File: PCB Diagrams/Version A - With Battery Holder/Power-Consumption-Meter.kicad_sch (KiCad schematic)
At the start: 36 parts, among them J1 Jack_DC, J10 01x02, J11 01x02, J12 01x02, J13 01x02, J2 01x02, J3 01x02, J4 USB_A, J5 Jack_DC, J6 Jack_DC, J7 USB_B_Mini, J8 USB_B_Micro, J9 01x04, SW1 SW_SPDT, SW2 SW_Push, U1 INA219_Module, U2 Display_5641BS

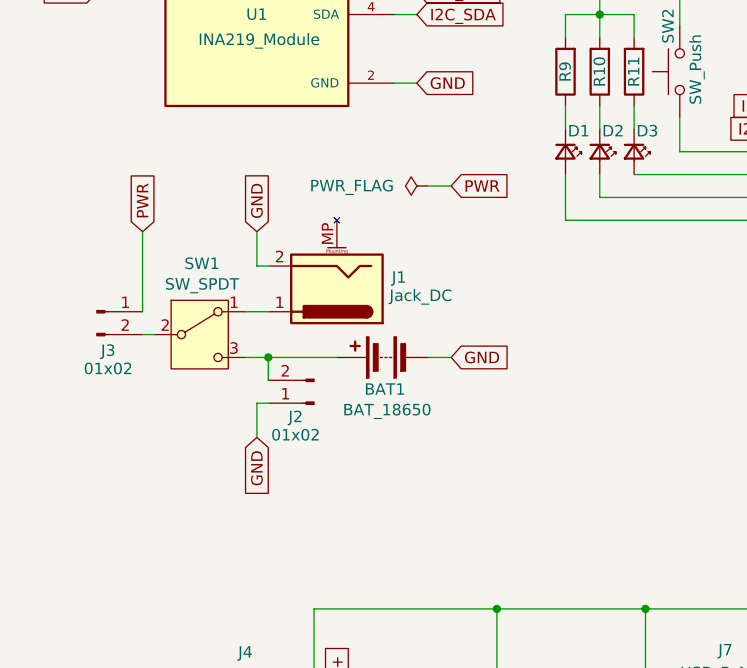
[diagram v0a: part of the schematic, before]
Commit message: update PCB connectors
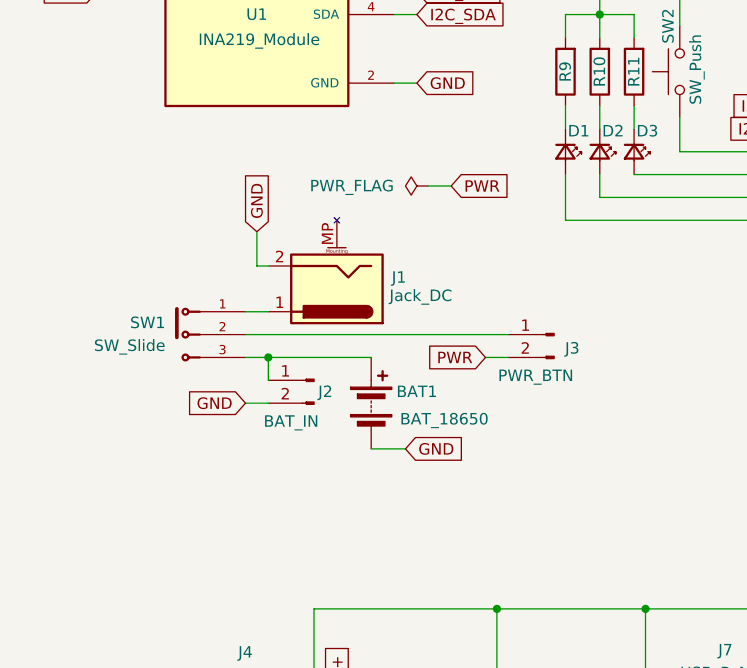
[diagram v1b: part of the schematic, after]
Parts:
- removed SW1: SW_SPDT, Button_Switch_THT:SW_Slide_SPDT_Straight_CK_OS102011MS2Q, symbol Switch:SW_SPDT
- added SW1: SW_Slide, Custom:Switch_Slide_SPDT_Straight_TE_1825159_1, symbol Custom:Switch_Slide_SPDT_Straight_TE_1825159_1
- J2: value 01x02 -> BAT_IN
- J3: value 01x02 -> PWR_BTN
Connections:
- net GND: now also J2.2 (Pin_2); no longer J2.1 (Pin_1)
- net PWR: now also J3.2 (Pin_2); no longer J3.1 (Pin_1)
- net at J1.1: now also SW1.1
- net at BAT1.1 (+): now also J2.1 (Pin_1), SW1.3; no longer J2.2 (Pin_2)
- new net: J3.1 (Pin_1), SW1.2
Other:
- moved on the sheet: BAT1, J2, J3

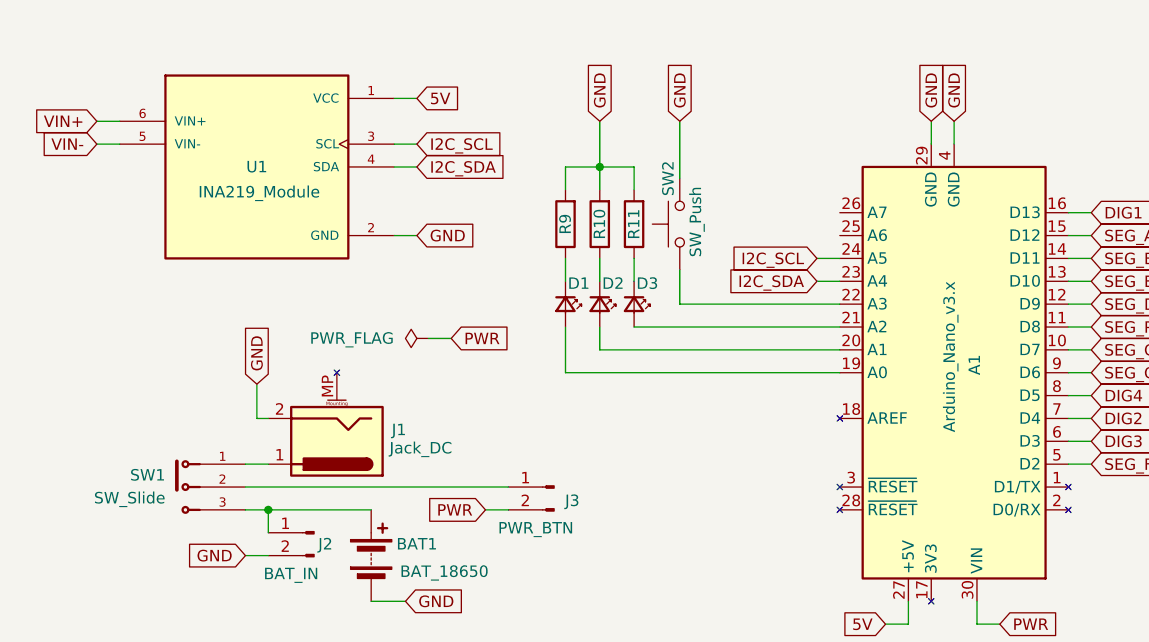
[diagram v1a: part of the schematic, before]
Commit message: Adding PCB building and assembly pictures
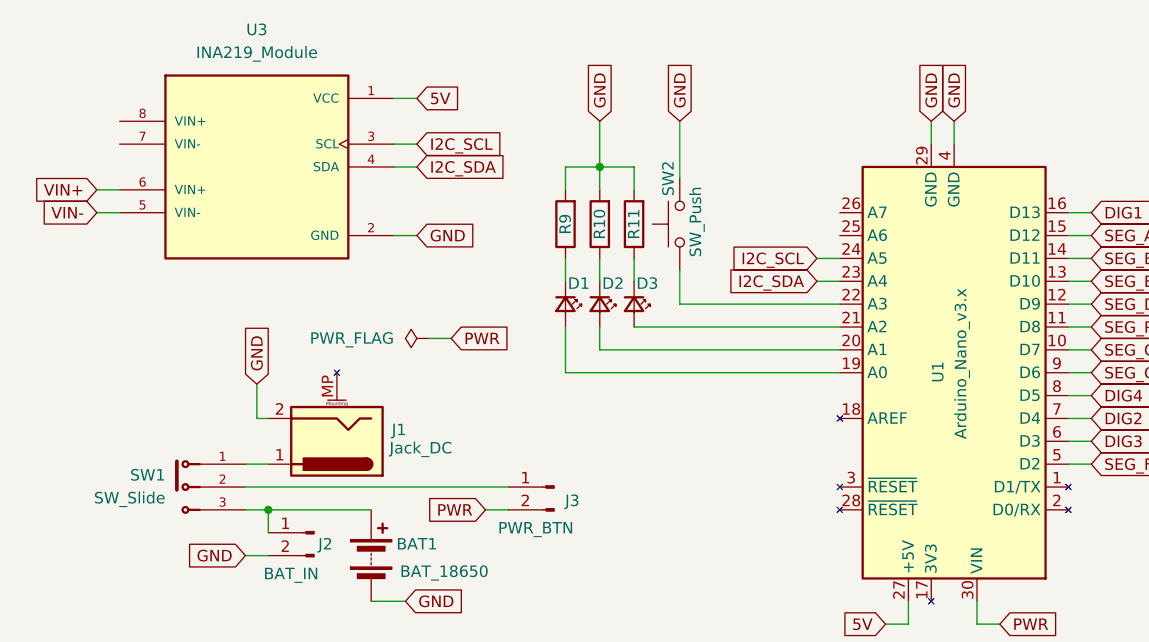
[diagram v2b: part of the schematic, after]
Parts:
- removed U1: INA219_Module, Custom:INA219_Module_Adafruit, symbol Custom:INA219_Module
- added U3: INA219_Module, Custom:INA219_Module_Generic, symbol Custom:INA219_Module_Adafruit
- renumbered A1 to U1
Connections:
- net 5V: now also U3.1 (VCC)
- net GND: now also U3.2 (GND)
- net I2C_SCL: now also U3.3 (SCL)
- net I2C_SDA: now also U3.4 (SDA)
- net VIN+: now also U3.6 (VIN+)
- net VIN-: now also U3.5 (VIN-)
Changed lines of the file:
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@@
 	(wire
 		(pts
-			(xy 45.72 40.64) (xy 48.26 40.64)
-		)
-		(stroke
-			(width 0)
-			(type default)
-		)
-	)
-	(wire
-		(pts
 			(xy 101.6 58.42) (xy 101.6 55.88)
 		)
@@
 	(wire
 		(pts
-			(xy 45.72 43.18) (xy 48.26 43.18)
-		)
-		(stroke
-			(width 0)
-			(type default)
-		)
-	)
-	(wire
-		(pts
 			(xy 110.49 57.15) (xy 110.49 60.96)
 		)
@@
 	(wire
 		(pts
+			(xy 45.72 50.8) (xy 48.26 50.8)
+		)
+		(stroke
+			(width 0)
+			(type default)
+		)
+	)
+	(wire
+		(pts
 			(xy 97.79 55.88) (xy 97.79 58.42)
 		)
@@
 	(wire
 		(pts
+			(xy 45.72 48.26) (xy 48.26 48.26)
+		)
+		(stroke
+			(width 0)
+			(type default)
+		)
+	)
+	(wire
+		(pts
 			(xy 90.17 111.76) (xy 106.68 111.76)
 		)
@@
 		)
 	)
-	(global_label "VIN+"
-		(shape input)
-		(at 45.72 40.64 180)
-		(fields_autoplaced yes)
-		(effects
-			(font
-				(size 1.27 1.27)
-			)
-			(justify right)
-		)
-		(property "Intersheetrefs" "${INTERSHEET_REFS}"
-			(at 38.1385 40.64 0)
-			(effects
-				(font
-					(size 1.27 1.27)
-				)
-				(justify right)
-				(hide yes)
-			)
-		)
-	)
-	(global_label "VIN-"
+	(global_label "SEG_G"
 		(shape input)
-		(at 45.72 43.18 180)
+		(at 156.21 68.58 0)
 		(fields_autoplaced yes)
 		(effects
@@
 				(size 1.27 1.27)
 			)
-			(justify right)
+			(justify left)
 		)
 		(property "Intersheetrefs" "${INTERSHEET_REFS}"
-			(at 38.1385 43.18 0)
+			(at 165.0613 68.58 0)
 			(effects
 				(font
 					(size 1.27 1.27)
 				)
-				(justify right)
+				(justify left)
 				(hide yes)
 			)
 		)
 	)
-	(global_label "SEG_G"
+	(global_label "I2C_SDA"
 		(shape input)
-		(at 156.21 68.58 0)
+		(at 81.28 45.72 0)
 		(fields_autoplaced yes)
 		(effects
@@
 		)
 		(property "Intersheetrefs" "${INTERSHEET_REFS}"
-			(at 165.0613 68.58 0)
+			(at 91.8852 45.72 0)
 			(effects
 				(font
@@
 		)
 	)
-	(global_label "I2C_SDA"
+	(global_label "VIN-"
 		(shape input)
-		(at 81.28 45.72 0)
+		(at 45.72 50.8 180)
 		(fields_autoplaced yes)
 		(effects
@@
 				(size 1.27 1.27)
 			)
-			(justify left)
+			(justify right)
 		)
 		(property "Intersheetrefs" "${INTERSHEET_REFS}"
-			(at 91.8852 45.72 0)
+			(at 38.1385 50.8 0)
 			(effects
 				(font
 					(size 1.27 1.27)
 				)
-				(justify left)
+				(justify right)
 				(hide yes)
 			)
@@
 		)
 	)
+	(global_label "VIN+"
+		(shape input)
+		(at 45.72 48.26 180)
+		(fields_autoplaced yes)
+		(effects
+			(font
+				(size 1.27 1.27)
+			)
+			(justify right)
+		)
+		(property "Intersheetrefs" "${INTERSHEET_REFS}"
+			(at 38.1385 48.26 0)
+			(effects
+				(font
+					(size 1.27 1.27)
+				)
+				(justify right)
+				(hide yes)
+			)
+		)
+	)
 	(global_label "SEG_A"
 		(shape input)
@@
 		(on_board yes)
 		(dnp no)
-		(property "Reference" "A1"
-			(at 143.256 66.548 90)
+		(property "Reference" "U1"
+			(at 139.192 67.31 90)
 			(effects
 				(font
@@
 		)
 		(property "Value" "Arduino_Nano_v3.x"
-			(at 140.462 58.42 90)
+			(at 141.732 59.182 90)
 			(effects
 				(font
@@
 			(project ""
 				(path "/04a21a1e-c762-45c9-8522-5107851ca11f"
-					(reference "A1")
+					(reference "U1")
 					(unit 1)
 				)
@@
 	)
 	(symbol
-		(lib_id "Custom:INA219_Module")
-		(at 63.5 45.72 0)
-		(unit 1)
-		(exclude_from_sim no)
-		(in_bom yes)
-		(on_board yes)
-		(dnp no)
-		(property "Reference" "U1"
-			(at 63.5 45.72 0)
-			(effects
-				(font
-					(size 1.27 1.27)
-				)
-			)
-		)
-		(property "Value" "INA219_Module"
-			(at 63.754 48.514 0)
-			(effects
-				(font
-					(size 1.27 1.27)
-				)
-			)
-		)
-		(property "Footprint" "Custom:INA219_Module_Adafruit"
-			(at 18.796 66.802 0)
-			(effects
-				(font
-					(size 1.27 1.27)
-				)
-				(justify bottom)
-				(hide yes)
-			)
-		)
-		(property "Datasheet" ""
-			(at 63.5 45.72 0)
-			(effects
-				(font
-					(size 1.27 1.27)
-				)
-				(hide yes)
-			)
-		)
-		(property "Description" ""
-			(at 63.5 45.72 0)
-			(effects
-				(font
-					(size 1.27 1.27)
-				)
-				(hide yes)
-			)
-		)
-		(property "MP" "INA219"
-			(at 11.176 64.262 0)
-			(effects
-				(font
-					(size 1.27 1.27)
-				)
-				(justify bottom)
-				(hide yes)
-			)
-		)
-		(property "SNAPEDA_PN" "INA219 High Side DC Current Sensor Breakout - 26V ±3.2A Max - STEMMA QT"
-			(at 46.228 69.596 0)
-			(effects
-				(font
-					(size 1.27 1.27)
-				)
-				(justify bottom)
-				(hide yes)
-			)
-		)
-		(pin "4"
-		)
-		(pin "3"
-		)
-		(pin "5"
-		)
-		(pin "6"
-		)
-		(pin "1"
-		)
-		(pin "SH1"
-		)
-		(pin "2"
-		)
-		(instances
-			(project ""
-				(path "/04a21a1e-c762-45c9-8522-5107851ca11f"
-					(reference "U1")
-					(unit 1)
-				)
-			)
-		)
-	)
-	(symbol
 		(lib_id "Device:R")
 		(at 97.79 52.07 180)
@@
 					(unit 1)
 				)
+			)
+		)
+	)
+	(symbol
+		(lib_id "Custom:INA219_Module_Adafruit")
+		(at 63.5 45.72 0)
+		(unit 1)
+		(exclude_from_sim no)
+		(in_bom yes)
+		(on_board yes)
+		(dnp no)
+		(fields_autoplaced yes)
+		(property "Reference" "U3"
+			(at 63.5 30.48 0)
+			(effects
+				(font
+					(size 1.27 1.27)
+				)
+			)
+		)
+		(property "Value" "INA219_Module"
+			(at 63.5 33.02 0)
+			(effects
+				(font
+					(size 1.27 1.27)
+				)
+			)
+		)
+		(property "Footprint" "Custom:INA219_Module_Generic"
+			(at 44.196 68.834 0)
+			(effects
+				(font
+					(size 1.27 1.27)
+				)
+				(justify bottom)
+				(hide yes)
+			)
+		)
+		(property "Datasheet" ""
+			(at 63.5 45.72 0)
+			(effects
+				(font
+					(size 1.27 1.27)
+				)
+				(hide yes)
+			)
+		)
+		(property "Description" ""
+			(at 63.5 45.72 0)
+			(effects
+				(font
+					(size 1.27 1.27)
+				)
+				(hide yes)
+			)
+		)
+		(property "MP" "INA219"
+			(at 36.576 66.294 0)
+			(effects
+				(font
+					(size 1.27 1.27)
+				)
+				(justify bottom)
+				(hide yes)
+			)
+		)
+		(property "SNAPEDA_PN" "INA219 High Side DC Current Sensor Breakout - 26V ±3.2A Max - STEMMA QT"
+			(at 71.628 71.628 0)
+			(effects
+				(font
+					(size 1.27 1.27)
+				)
+				(justify bottom)
+				(hide yes)
+			)
+		)
+		(pin "6"
+		)
+		(pin "5"
+		)
+		(pin "1"
+		)
+		(pin "3"
+		)
+		(pin "4"
+		)
+		(pin "7"
+		)
+		(pin "8"
+		)
+		(pin "2"
+		)
+		(instances
+			(project ""
+				(path "/04a21a1e-c762-45c9-8522-5107851ca11f"
+					(reference "U3")
+					(unit 1)
+				)
